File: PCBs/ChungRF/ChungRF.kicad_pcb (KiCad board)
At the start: 4 copper layers, 28.4 x 53.4 mm, 15 parts, among them J1 Conn_Coaxial, J2 Conn_01x09_Socket, U1 E22-900M30S

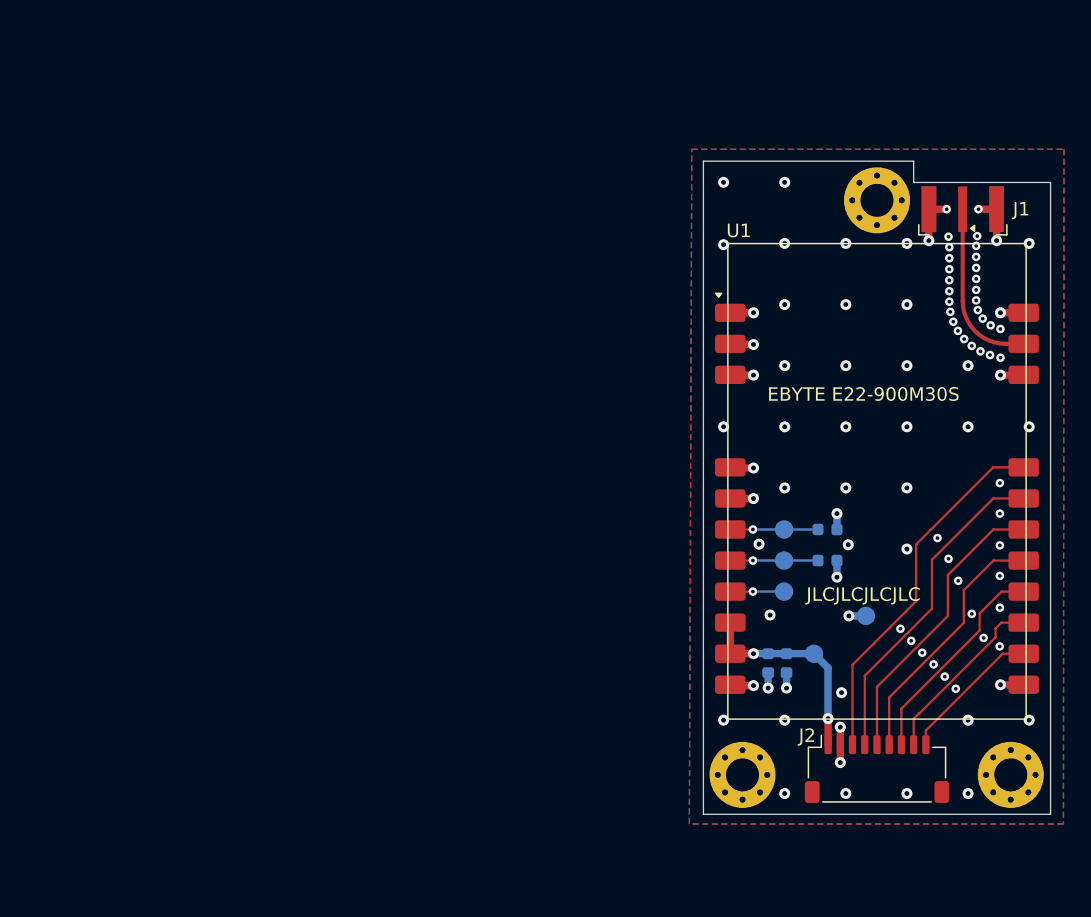
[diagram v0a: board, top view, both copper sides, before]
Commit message: Add ESP32-S3-MINI
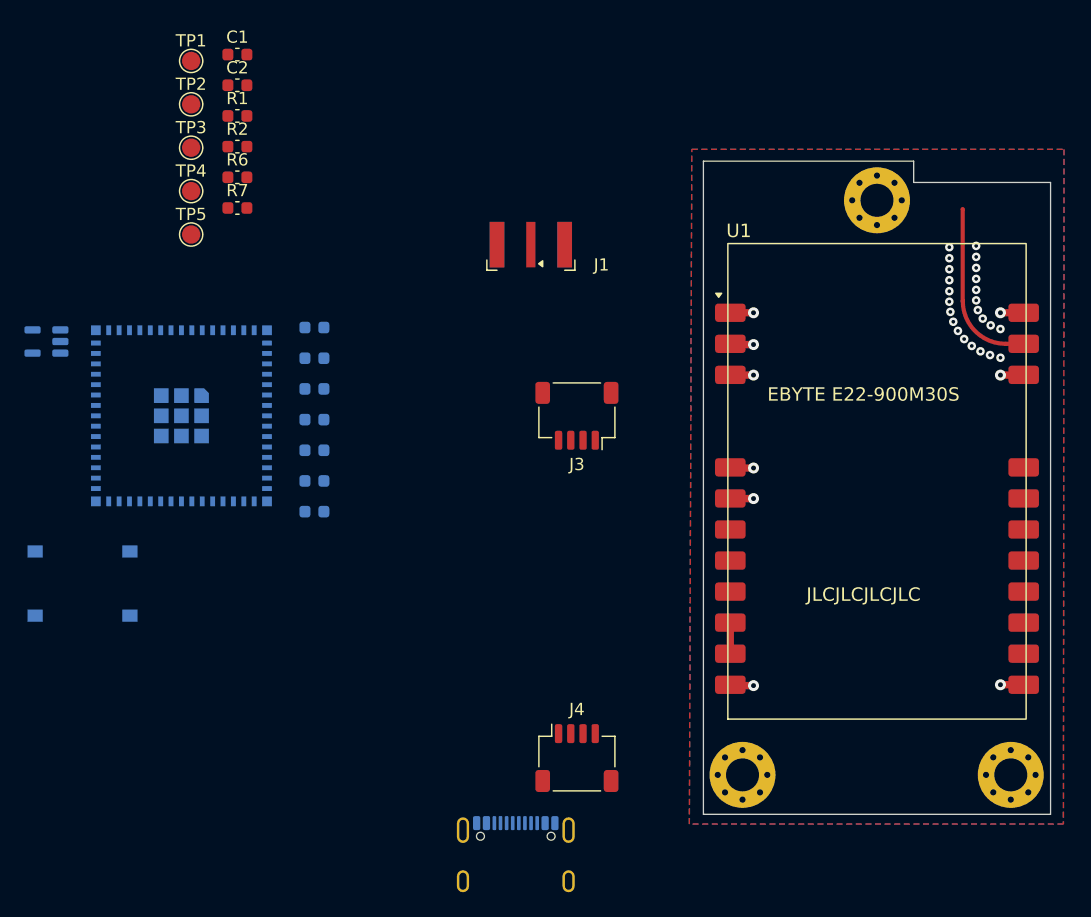
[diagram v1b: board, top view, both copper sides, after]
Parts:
- added C3: 1uF, Capacitor_SMD:C_0603_1608Metric, B.Cu at (119.5, 74.8)
- added C4: 10uf, Capacitor_SMD:C_0603_1608Metric, B.Cu at (119.5, 77.3)
- added C5: 10uf, Capacitor_SMD:C_0603_1608Metric, B.Cu at (119.5, 79.8)
- added C6: 10uf, Capacitor_SMD:C_0603_1608Metric, B.Cu at (119.5, 82.3)
- added J3: JST-SM04B-SRSS, besser_footprints:JST_SH_SM04B-SRSS-TB_1x04-1MP_P1.00mm_Horizontal, F.Cu at (141.0, 82.0)
- added J4: JST-SM04B-SRSS, besser_footprints:JST_SH_SM04B-SRSS-TB_1x04-1MP_P1.00mm_Horizontal, F.Cu at (141.0, 110.0)
- added R3: 5.1K, Capacitor_SMD:C_0603_1608Metric, B.Cu at (119.5, 84.8)
- added R4: 5.1k, Capacitor_SMD:C_0603_1608Metric, B.Cu at (119.5, 87.3)
- added R5: 5.1k, Capacitor_SMD:C_0603_1608Metric, B.Cu at (119.5, 89.8)
- added R6: 5.1k, Capacitor_SMD:C_0603_1608Metric, F.Cu at (113.2, 62.5)
- added R7: 5.1k, Capacitor_SMD:C_0603_1608Metric, F.Cu at (113.2, 65.0)
- added SW1: PTS636 SK25F, Button_Switch_SMD:SW_Tactile_SPST_NO_Straight_CK_PTS636Sx25SMTRLFS, B.Cu at (100.6, 93.1)
- added SW2: PTS636 SK25F, Button_Switch_SMD:SW_Tactile_SPST_NO_Straight_CK_PTS636Sx25SMTRLFS, B.Cu at (100.6, 98.3)
- added U2: ESP32-S3-MINI-1U, RF_Module:ESP32-S2-MINI-1U, B.Cu at (108.7, 82.0)
- added U3: AP2112K-3.3TRG1, Package_TO_SOT_SMD:SOT-23-5, B.Cu at (97.6, 75.9)
- C1, C2, TP1, TP2, TP3, TP4, TP5: moved to F.Cu
- J2: value Conn_01x09_Socket -> USB4105-GF-A; footprint Connector_JST:JST_SH_SM09B-SRSS-TB_1x09-1MP_P1.00mm_Horizontal -> Connector_USB:USB_C_Receptacle_GCT_USB4105-xx-A_16P_TopMnt_Horizontal; moved to B.Cu
- R1, R2: value 100k -> 10k; moved to F.Cu
- moved TP1 70.3 mm to (109.4, 53.0), turned to 0 degrees
- moved TP2 69.3 mm to (109.4, 56.5), turned to 0 degrees
- moved C1 66.1 mm to (113.2, 52.5), turned to 0 degrees
- moved C2 65.2 mm to (113.2, 55.0), turned to 0 degrees
- moved R2 59.0 mm to (113.2, 60.0)
- moved R1 58.9 mm to (113.2, 57.5), turned to 0 degrees
- moved TP3 57.7 mm to (109.4, 60.1), turned to 0 degrees
- moved TP4 57.1 mm to (109.4, 63.6), turned to 0 degrees
- moved TP5 56.6 mm to (109.4, 67.2), turned to 0 degrees
- moved J1 35.5 mm to (137.2, 68.0)
- moved J2 30.6 mm to (136.0, 119.0), turned to 180 degrees
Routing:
- net /NSS: track 29.9 -> 0.00 mm
- net /SCK: track 27.0 -> 0.00 mm
- net /MOSI: track 24.0 -> 0.00 mm
- net /MISO: track 21.1 -> 0.00 mm
- net /NRST: track 17.7 -> 0.00 mm
- net GND: track 34.6 -> 17.1 mm, vias 99 -> 33
- net /BUSY: track 14.8 -> 0.00 mm
- net VCC: track 17.2 -> 2.54 mm, vias 2 -> 0
- net /DIO1: track 11.8 -> 0.00 mm
- net /TXEN: track 7.18 -> 0.00 mm, vias 1 -> 0
- net /RXEN: track 7.18 -> 0.00 mm, vias 1 -> 0
- net /DIO2: track 4.40 -> 0.00 mm, vias 1 -> 0
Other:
- board text removed: "DIO2"
- board text removed: "GND"
- board text removed: "RXEN"
- board text removed: "TXEN"
- board text removed: "VCC"

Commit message: ChungRF R2
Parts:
- removed C4, C5, C6: 10uf, Capacitor_SMD:C_0603_1608Metric
- removed H3: MountingHole, MountingHole:MountingHole_2.7mm_M2.5_Pad_Via
- removed J3, J4: JST-SM04B-SRSS, besser_footprints:JST_SH_SM04B-SRSS-TB_1x04-1MP_P1.00mm_Horizontal
- removed R3: 5.1K, Capacitor_SMD:C_0603_1608Metric
- removed R4, R5, R6, R7: 5.1k, Capacitor_SMD:C_0603_1608Metric
- removed SW1, SW2: PTS636 SK25F, Button_Switch_SMD:SW_Tactile_SPST_NO_Straight_CK_PTS636Sx25SMTRLFS
- removed TP1: VCC, TestPoint:TestPoint_Pad_D1.5mm
- removed TP2: GND, TestPoint:TestPoint_Pad_D1.5mm
- removed TP3: RXEN, TestPoint:TestPoint_Pad_D1.5mm
- removed TP4: TXEN, TestPoint:TestPoint_Pad_D1.5mm
- removed TP5: DIO2, TestPoint:TestPoint_Pad_D1.5mm
- removed the U2 at (108.7, 82.0)
- removed U3: AP2112K-3.3TRG1, Package_TO_SOT_SMD:SOT-23-5
- added U1: KB2040, besser_footprints:Adafuit-KB2040-SMD, B.Cu at (168.1, 96.7)
- C1, C2, R1, R2: moved to B.Cu
- C3: value 1uF -> 10uF
- H1, H2: value MountingHole -> 2.7mm_M2.5_Pad_Via
- J1: value Conn_Coaxial -> JST-SM04B-SRSS; footprint besser_footprints:CON-SMA-EDGE-S -> besser_footprints:JST_SH_SM04B-SRSS-TB_1x04-1MP_P1.00mm_Horizontal
- J2: value USB4105-GF-A -> Conn_Coaxial; footprint Connector_USB:USB_C_Receptacle_GCT_USB4105-xx-A_16P_TopMnt_Horizontal -> besser_footprints:CONSMA003.062; moved to F.Cu
- moved J2 65.0 mm to (172.6, 65.2), turned to 0 degrees
- moved C1 64.5 mm to (154.9, 101.7)
- moved C2 61.5 mm to (154.9, 100.2)
- moved R2 53.7 mm to (154.9, 93.8)
- moved R1 53.7 mm to (154.9, 91.3), turned to 180 degrees
- moved J1 51.1 mm to (165.5, 110.5)
- moved H1 48.0 mm to (165.5, 64.7), turned to 0 degrees
- moved C3 42.7 mm to (154.9, 98.7), turned to 0 degrees
- moved H2 22.0 mm to (154.5, 110.6), turned to 0 degrees
- renumbered U1 to U2
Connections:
- C1 pad 1: VCC -> VBUS
- C2 pad 1: VCC -> VBUS
- C3 pad 1: /RESET -> VBUS
- J1 pad 1: /RF_ANT -> GND
- J1 pad 2: GND -> VBUS
- U2 pad 10: VCC -> VBUS
- U2 pad 9: VCC -> VBUS
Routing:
- net VBUS: track 0.00 -> 31.3 mm, vias 0 -> 3
- net GND: track 17.1 -> 39.3 mm, vias 33 -> 79
- net /NSS: track 0.00 -> 11.9 mm, vias 0 -> 1
- net /SCK: track 0.00 -> 11.8 mm, vias 0 -> 1
- net /NRST: track 0.00 -> 11.5 mm, vias 0 -> 1
- net /MOSI: track 0.00 -> 11.4 mm, vias 0 -> 1
- net /MISO: track 0.00 -> 11.4 mm, vias 0 -> 1
- net /BUSY: track 0.00 -> 11.4 mm, vias 0 -> 1
- net /DIO1: track 0.00 -> 11.4 mm, vias 0 -> 1
- net /CARFIO_MOSI: track 0.00 -> 9.41 mm, vias 0 -> 1
- net /CARFIO_MISO: track 0.00 -> 8.08 mm, vias 0 -> 1
- net /DIO2: track 0.00 -> 5.91 mm, vias 0 -> 1
- net /TXEN: track 0.00 -> 4.88 mm, vias 0 -> 1
- net /RXEN: track 0.00 -> 3.52 mm, vias 0 -> 1
- net VCC: track 2.54 -> 0.00 mm
- added copper zone on B.Cu, net VBUS
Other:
- board size 28.4 x 53.4 mm -> 28.4 x 52.3 mm
- board text added: "ANT"
- board text added: "CARFIO"
- board text added: "R2 6-2024"
- board text removed: "Chungus Aerospace"
- board text removed: "EBYTE E22-900M30S"
- board text removed: "R2 5-2024"
